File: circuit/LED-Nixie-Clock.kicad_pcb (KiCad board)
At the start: 2 copper layers, 214.6 x 43.2 mm, 197 parts, among them J1 USB Micro, J2 Debug, J3 Serial, SW1 Boot0, U1 MCP1700-3302E_SOT23, U2 STM32F103C8Tx, Y1 8MHz, Y2 32.768kHz

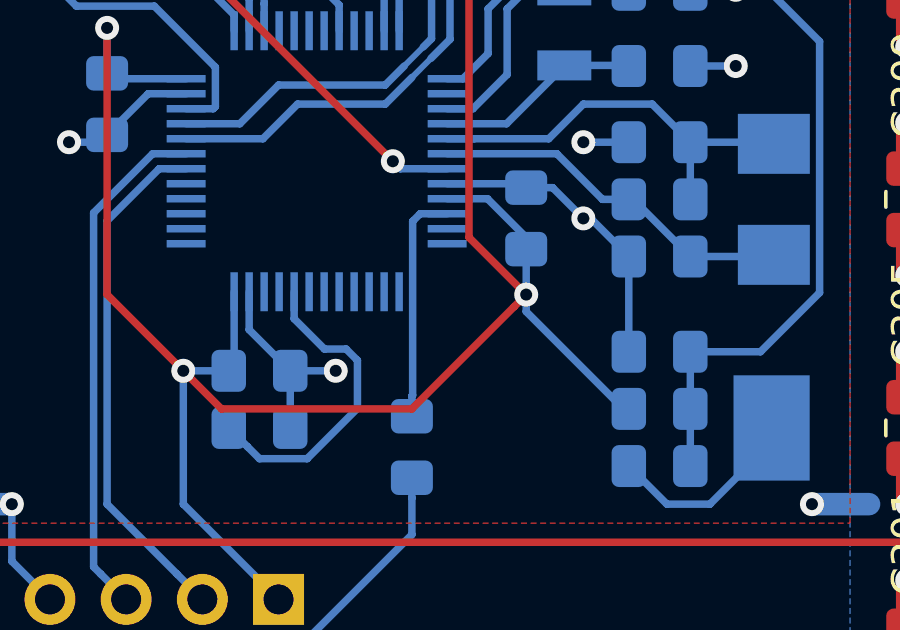
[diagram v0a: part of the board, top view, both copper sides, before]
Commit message: Move LED data bus to PA2 (which is on the same pin as USART2 Tx)
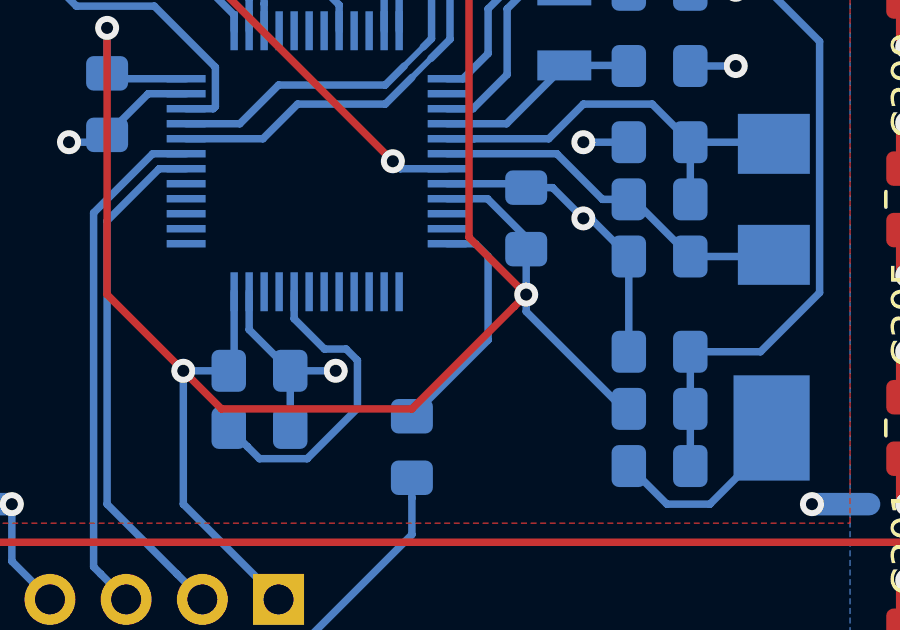
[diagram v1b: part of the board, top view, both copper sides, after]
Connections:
- U2 pad 10: Net-(R8-Pad2) -> (no net)
- U2 pad 12: (no net) -> Net-(R8-Pad2)

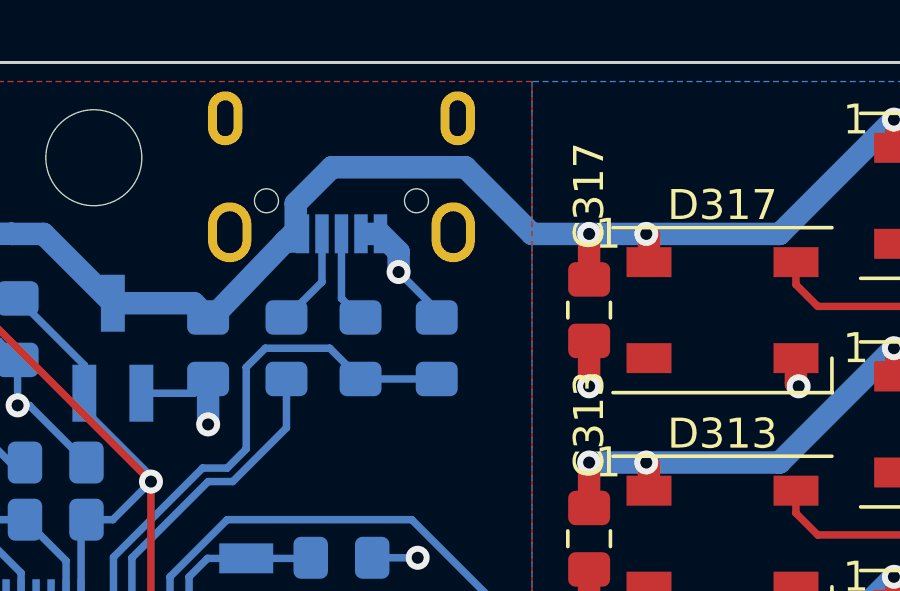
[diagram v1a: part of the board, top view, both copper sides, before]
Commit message: Fix USBDP pull up resistor
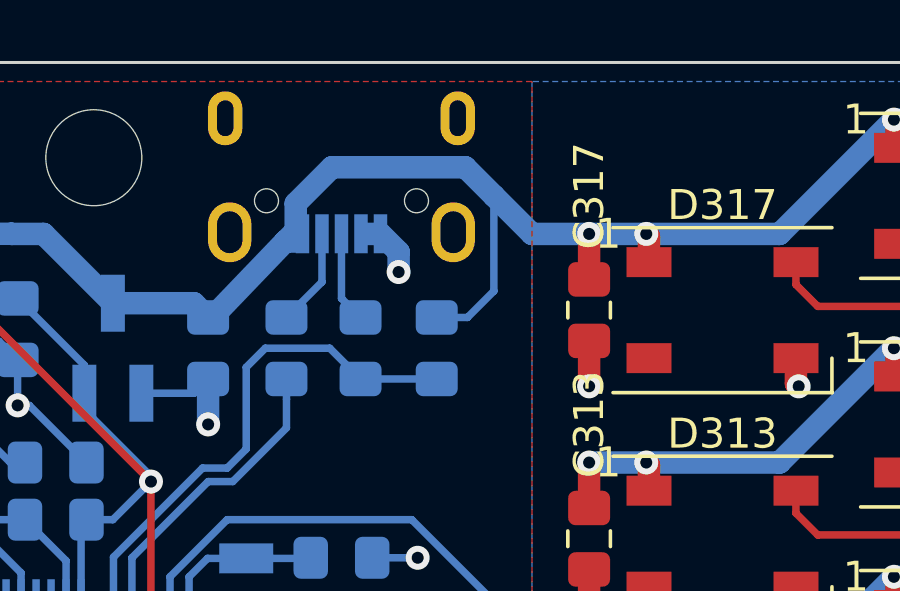
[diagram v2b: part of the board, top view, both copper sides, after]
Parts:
- turned R3 to 90 degrees
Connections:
- R3 pad 1: GND -> /USBDP
- R3 pad 2: /USBDP -> VBUS
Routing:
- net VBUS: track 1246.5 -> 1252.0 mm
- net GND: track 263.6 -> 261.5 mm
- net /USBDP: track 26.1 -> 26.7 mm
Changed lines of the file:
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@@
     (thickness 1.6)
     (drawings 262)
-    (tracks 1849)
+    (tracks 1851)
     (zones 0)
     (modules 197)
@@
   )
   (module Resistor_SMD:R_0805_2012Metric_Pad1.15x1.40mm_HandSolder (layer B.Cu)
-    (at 167.005 83.82 270)
+    (at 167.005 83.82 90)
     (descr "Resistor SMD 0805 (2012 Metric), square (rectangular) end terminal, IPC_7351 nominal with elongated pad for handsoldering. (Body size source: https://docs.google.com/spreadsheets/d/1BsfQQcO9C6DZCsRaXUlFlo91Tg2WpOkGARC1WS5S8t0/edit?usp=sharing), generated with kicad-footprint-generator")
     (tags "resistor handsolder")
     (attr smd)
-    (fp_text reference R3 (at 2.54 0 270) (layer B.SilkS)
+    (fp_text reference R3 (at 2.54 0 90) (layer B.SilkS)
       (effects (font (size 1 1) (thickness 0.15)) (justify mirror))
     )
-    (fp_text value 4.7k (at 0 -1.65 270) (layer B.Fab)
+    (fp_text value 4.7k (at 0 -1.65 90) (layer B.Fab)
       (effects (font (size 1 1) (thickness 0.15)) (justify mirror))
     )
@@
     (fp_line (start 1.85 0.95) (end 1.85 -0.95) (layer B.CrtYd) (width 0.05))
     (fp_line (start 1.85 -0.95) (end -1.85 -0.95) (layer B.CrtYd) (width 0.05))
-    (fp_text user %R (at 0 0 270) (layer B.Fab)
+    (fp_text user %R (at 0 0 90) (layer B.Fab)
       (effects (font (size 0.5 0.5) (thickness 0.08)) (justify mirror))
     )
-    (pad 1 smd roundrect (at -1.025 0 270) (size 1.15 1.4) (layers B.Cu B.Paste B.Mask) (roundrect_rratio 0.217391)
-      (net 1 GND))
-    (pad 2 smd roundrect (at 1.025 0 270) (size 1.15 1.4) (layers B.Cu B.Paste B.Mask) (roundrect_rratio 0.217391)
+    (pad 1 smd roundrect (at -1.025 0 90) (size 1.15 1.4) (layers B.Cu B.Paste B.Mask) (roundrect_rratio 0.217391)
       (net 52 /USBDP))
+    (pad 2 smd roundrect (at 1.025 0 90) (size 1.15 1.4) (layers B.Cu B.Paste B.Mask) (roundrect_rratio 0.217391)
+      (net 51 VBUS))
     (model ${KISYS3DMOD}/Resistor_SMD.3dshapes/R_0805_2012Metric.wrl
       (at (xyz 0 0 0))
@@
   (segment (start 159.385 84.845) (end 159.385 86.36) (width 0.75) (layer B.Cu) (net 1) (status 10))
   (via (at 165.735 81.28) (size 0.8) (drill 0.4) (layers F.Cu B.Cu) (net 1))
+  (segment (start 165.735 81.28) (end 165.735 80.61) (width 0.75) (layer B.Cu) (net 1))
+  (segment (start 165.735 80.61) (end 165.13 80.005) (width 0.75) (layer B.Cu) (net 1))
   (via (at 168.91 107.95) (size 0.8) (drill 0.4) (layers F.Cu B.Cu) (net 1))
   (segment (start 162.805 95.885) (end 161.29 95.885) (width 0.25) (layer B.Cu) (net 1) (status 10))
@@
   (segment (start 164.67 90.805) (end 165.345 90.805) (width 0.25) (layer B.Cu) (net 1))
   (segment (start 165.325 93.325) (end 165.345 93.345) (width 0.25) (layer B.Cu) (net 1))
-  (segment (start 165.735 80.61) (end 165.13 80.005) (width 0.75) (layer B.Cu) (net 1))
-  (segment (start 165.735 81.28) (end 165.735 80.61) (width 0.75) (layer B.Cu) (net 1))
   (segment (start 164.6555 80.01) (end 165.1 80.01) (width 0.75) (layer B.Cu) (net 1))
-  (segment (start 167.005 82.55) (end 165.735 81.28) (width 0.25) (layer B.Cu) (net 1))
-  (segment (start 167.005 82.795) (end 167.005 82.55) (width 0.25) (layer B.Cu) (net 1))
   (segment (start 158.91 85.32) (end 159.385 84.845) (width 0.25) (layer B.Cu) (net 1))
   (segment (start 157.16 85.32) (end 158.91 85.32) (width 0.25) (layer B.Cu) (net 1))
@@
   (segment (start 162.305001 78.994999) (end 162.305001 79.909399) (width 0.75) (layer B.Cu) (net 51) (status 20))
   (segment (start 163.5125 77.7875) (end 162.305001 78.994999) (width 0.75) (layer B.Cu) (net 51))
-  (segment (start 170.18 80.01) (end 167.9575 77.7875) (width 0.75) (layer B.Cu) (net 51))
   (segment (start 167.9575 77.7875) (end 163.5125 77.7875) (width 0.75) (layer B.Cu) (net 51))
   (segment (start 172.085 80.01) (end 170.18 80.01) (width 0.75) (layer B.Cu) (net 51))
@@
   (segment (start 149.438266 80.00499) (end 150.771734 80.00499) (width 0.75) (layer B.Cu) (net 51))
   (segment (start 149.433256 80.01) (end 149.438266 80.00499) (width 0.75) (layer B.Cu) (net 51))
-  (segment (start 164.465 84.845) (end 166.37 84.845) (width 0.25) (layer B.Cu) (net 52) (status 30))
+  (segment (start 168.91 78.74) (end 167.9575 77.7875) (width 0.75) (layer B.Cu) (net 51))
+  (segment (start 170.18 80.01) (end 168.91 78.74) (width 0.75) (layer B.Cu) (net 51))
+  (segment (start 168.91 81.915) (end 168.91 78.74) (width 0.25) (layer B.Cu) (net 51))
+  (segment (start 168.03 82.795) (end 168.91 81.915) (width 0.25) (layer B.Cu) (net 51))
+  (segment (start 167.005 82.795) (end 168.03 82.795) (width 0.25) (layer B.Cu) (net 51))
   (segment (start 148.05 95.27) (end 149.84 95.27) (width 0.25) (layer B.Cu) (net 52) (status 10))
   (segment (start 151.13 93.98) (end 154.686 93.98) (width 0.25) (layer B.Cu) (net 52))
@@
   (segment (start 156.23001 92.43458) (end 155.956 92.70859) (width 0.25) (layer B.Cu) (net 52))
   (segment (start 160.655 87.179989) (end 160.02 87.814989) (width 0.25) (layer B.Cu) (net 52))
+  (segment (start 164.465 84.845) (end 167.005 84.845) (width 0.25) (layer B.Cu) (net 52))
   (segment (start 163.83 82.16) (end 164.465 82.795) (width 0.25) (layer B.Cu) (net 53) (status 20))
   (segment (start 163.83 80.005) (end 163.83 82.16) (width 0.25) (layer B.Cu) (net 53) (status 10))

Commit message: Update schematic and PCB to KiCad 5.1
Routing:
- net /Digit 1/DIN: track 115.4 -> 116.1 mm
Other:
- net class Power: trace_width 0.75 -> 0.5

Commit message: Adjust credits text on PCB
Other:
- board text added: "LED Nixie Clock"
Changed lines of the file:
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@@
   (general
     (thickness 1.6)
-    (drawings 262)
+    (drawings 263)
     (tracks 1849)
     (zones 0)
@@
     )
   )
+  (gr_text "LED Nixie Clock" (at 140.462 114.046) (layer B.SilkS)
+    (effects (font (size 1 0.5) (thickness 0.1)) (justify left mirror))
+  )
   (gr_line (start 89.75 81.15) (end 89.75 83.95) (layer Dwgs.User) (width 0.2))
   (gr_line (start 49.95 81.15) (end 89.75 81.15) (layer Dwgs.User) (width 0.2))
@@
   (gr_line (start 145.415 79.8195) (end 145.415 90.3605) (layer Dwgs.User) (width 0.1))
   (gr_line (start 143.8275 85.09) (end 146.8755 85.09) (layer Dwgs.User) (width 0.1))
-  (gr_text github.com/zargony/led-nixie-clock (at 133.35 115.57) (layer B.SilkS)
-    (effects (font (size 1 0.5) (thickness 0.1)) (justify mirror))
+  (gr_text github.com/zargony/led-nixie-clock (at 140.462 115.57) (layer B.SilkS)
+    (effects (font (size 1 0.5) (thickness 0.1)) (justify left mirror))
   )
   (gr_line (start 220.98 74.295) (end 220.98 117.475) (layer F.CrtYd) (width 0.1))

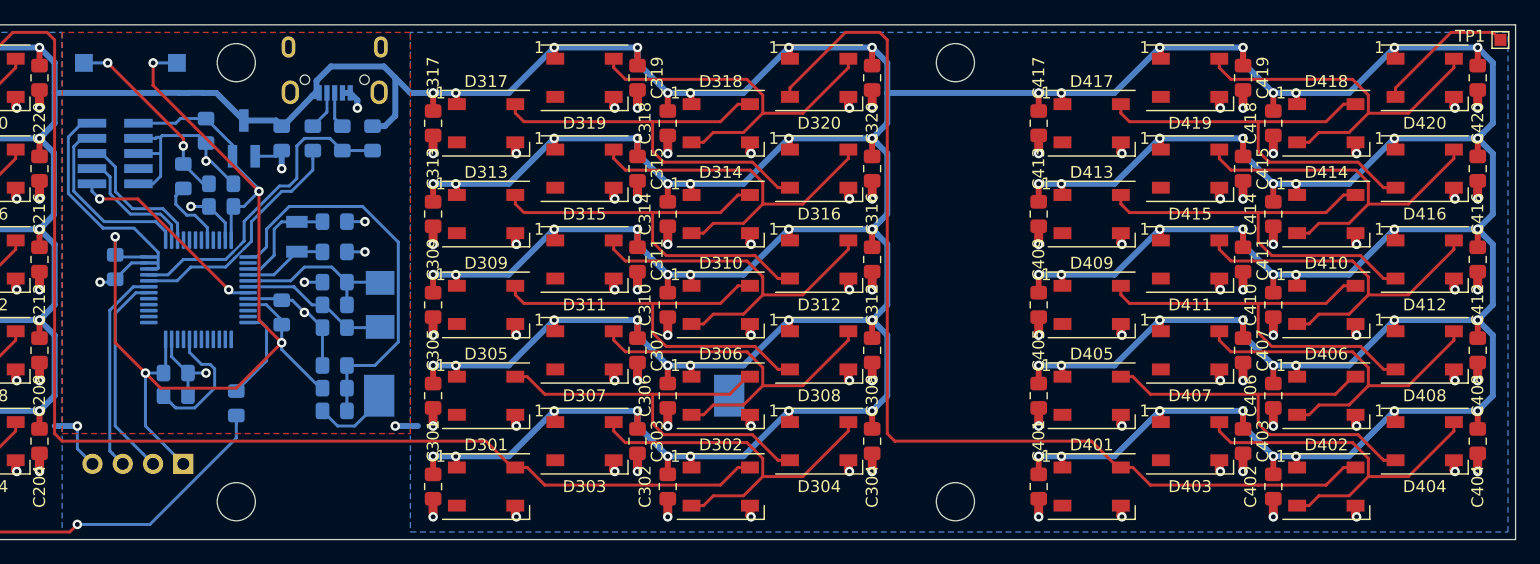
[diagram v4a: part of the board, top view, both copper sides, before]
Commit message: Add test points for DIN and DOUT, improve front side routing
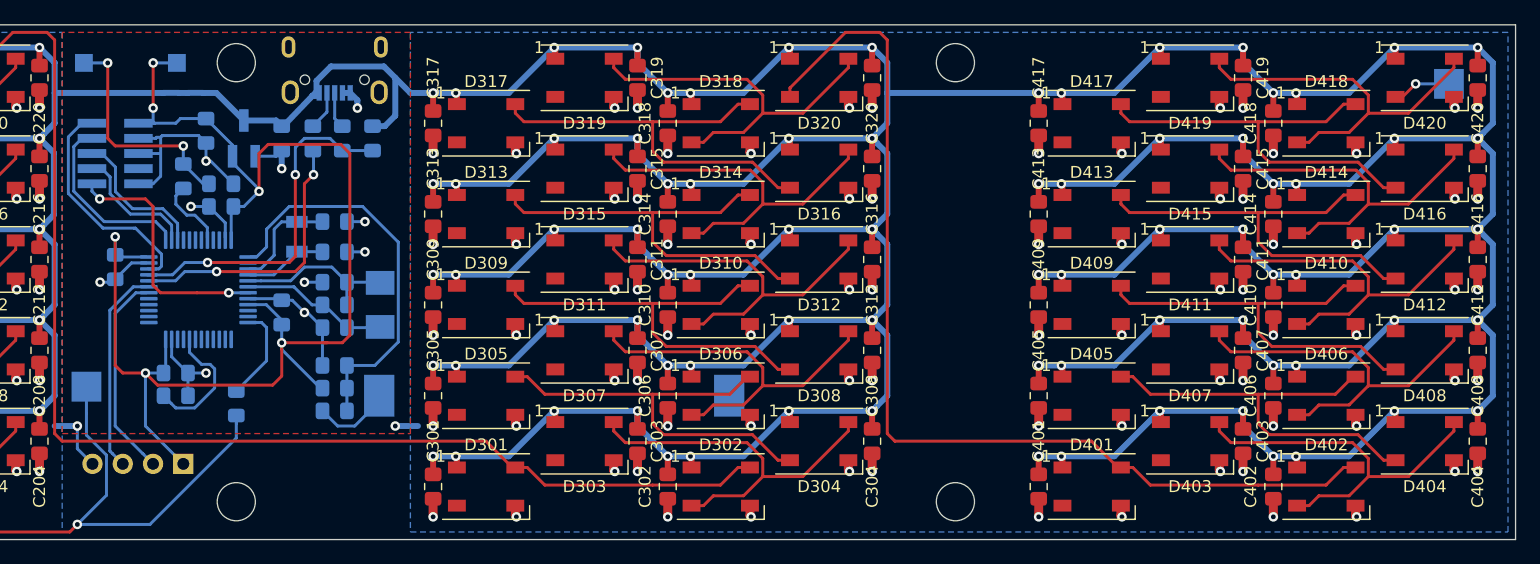
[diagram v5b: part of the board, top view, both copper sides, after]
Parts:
- removed TP1: DOUT, TestPoint:TestPoint_Pad_1.0x1.0mm
- added DIN: DIN, TestPoint:TestPoint_Pad_2.5x2.5mm, B.Cu at (143.0, 104.6)
- added DOUT: DOUT, TestPoint:TestPoint_Pad_2.5x2.5mm, B.Cu at (257.3, 79.2)
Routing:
- net /Digit 1/DIN: track 116.1 -> 129.4 mm
- net VDD: track 102.9 -> 115.5 mm, vias 5 -> 6
- net /Digit 4/DOUT: track 11.7 -> 4.93 mm, vias 0 -> 1
- net /RESET: track 17.4 -> 21.3 mm
- net Net-(R5-Pad2): track 15.9 -> 19.3 mm
- net /USBDM: track 20.4 -> 23.6 mm, vias 0 -> 2
- net /USBDP: track 26.7 -> 29.5 mm, vias 0 -> 2

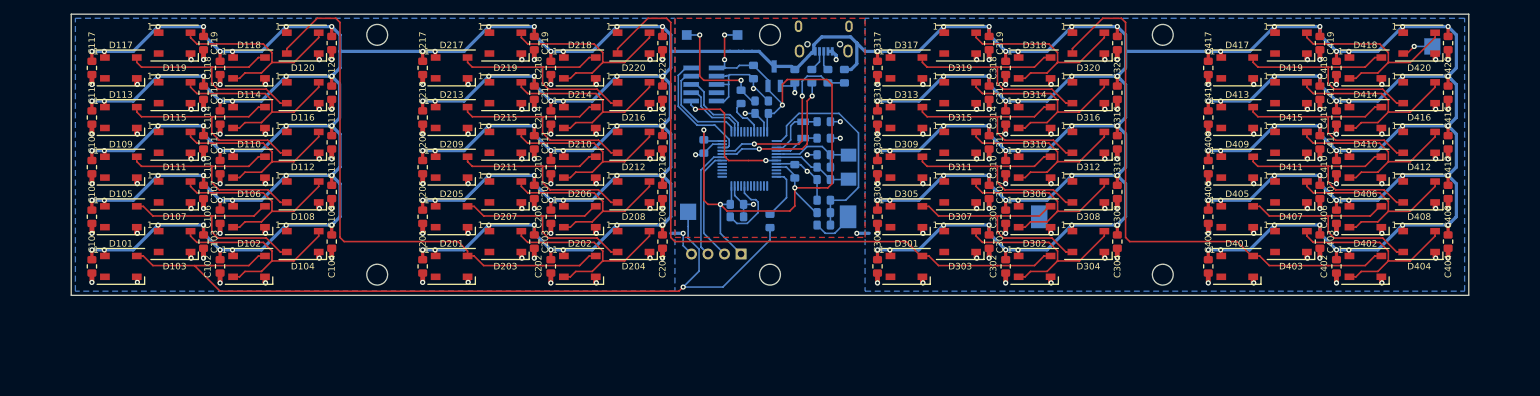
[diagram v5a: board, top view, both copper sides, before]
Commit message: Add input buttons
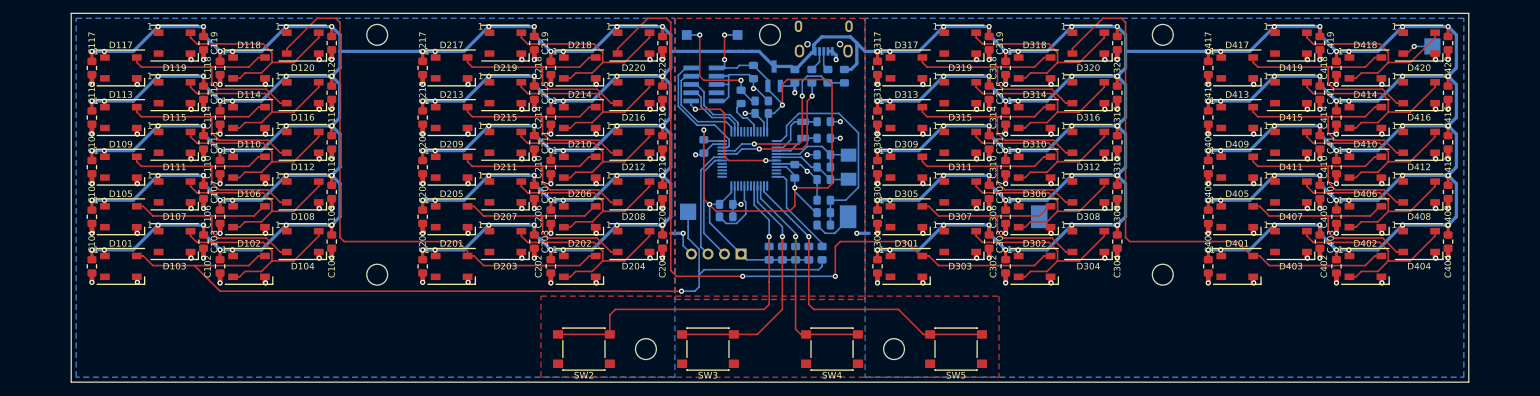
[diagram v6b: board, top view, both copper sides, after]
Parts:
- removed DIN: DIN, TestPoint:TestPoint_Pad_2.5x2.5mm
- added H7: MountingHole, MountingHole:MountingHole_3.2mm_M3_ISO7380, F.Cu at (174.6, 125.7)
- added R10: 100k, Resistor_SMD:R_0805_2012Metric_Pad1.15x1.40mm_HandSolder, B.Cu at (157.5, 111.0)
- added R11: 100k, Resistor_SMD:R_0805_2012Metric_Pad1.15x1.40mm_HandSolder, B.Cu at (159.5, 111.0)
- added R12: 100k, Resistor_SMD:R_0805_2012Metric_Pad1.15x1.40mm_HandSolder, B.Cu at (161.5, 111.0)
- added R9: 100k, Resistor_SMD:R_0805_2012Metric_Pad1.15x1.40mm_HandSolder, B.Cu at (155.4, 111.0)
- added SW2: Button "Back", Button_Switch_SMD:SW_Push_1P1T_NO_6x6mm_H9.5mm, F.Cu at (127.0, 125.7)
- added SW3: Button "-", Button_Switch_SMD:SW_Push_1P1T_NO_6x6mm_H9.5mm, F.Cu at (146.1, 125.7)
- added SW4: Button "+", Button_Switch_SMD:SW_Push_1P1T_NO_6x6mm_H9.5mm, F.Cu at (165.1, 125.7)
- added SW5: Button "Ok", Button_Switch_SMD:SW_Push_1P1T_NO_6x6mm_H9.5mm, F.Cu at (184.2, 125.7)
- added TP1: DIN, TestPoint:TestPoint_Pad_2.5x2.5mm, B.Cu at (143.0, 104.6)
- moved H6 80.2 mm to (136.5, 125.7)
- moved H2 70.7 mm to (155.6, 77.5)
- moved H3 60.3 mm to (215.9, 77.5)
- moved H4 60.3 mm to (95.2, 114.3)
- moved H5 36.8 mm to (215.9, 114.3)
- moved R8 9.41 mm to (163.6, 111.0)
- moved C7 1.65 mm to (148.8, 103.5)
- moved R7 1.65 mm to (148.8, 105.4)
- renumbered DOUT to TP2
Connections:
- U2 pad 14: (no net) -> /BTN3
- U2 pad 15: (no net) -> /BTN2
- U2 pad 16: (no net) -> /BTN1
- U2 pad 17: (no net) -> /BTN0
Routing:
- net /BTN0: track 0.00 -> 56.7 mm, vias 0 -> 1
- net /BTN3: track 0.00 -> 51.0 mm, vias 0 -> 1
- net /BTN1: track 0.00 -> 39.1 mm, vias 0 -> 1
- net /BTN2: track 0.00 -> 35.6 mm, vias 0 -> 1
- net VDD: track 115.5 -> 127.7 mm
- net /Digit 3/DIN: track 104.9 -> 114.9 mm, vias 0 -> 2
- net Net-(R8-Pad2): track 7.92 -> 14.3 mm
- net /Digit 1/DIN: track 129.4 -> 132.9 mm
- net /BOOT1: track 10.6 -> 9.46 mm
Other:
- board size 214.6 x 43.2 mm -> 214.6 x 56.6 mm

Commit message: Enlarge PCB and add more mounting holes
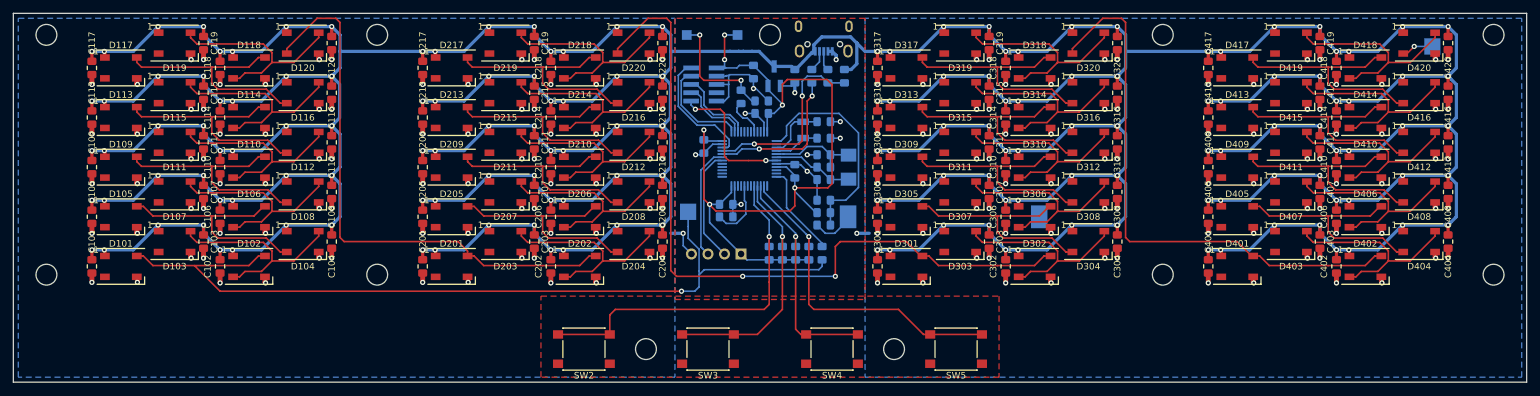
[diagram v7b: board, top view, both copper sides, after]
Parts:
- added H1: MountingHole, MountingHole:MountingHole_3.2mm_M3_ISO7380, F.Cu at (44.5, 77.5)
- added H5: MountingHole, MountingHole:MountingHole_3.2mm_M3_ISO7380, F.Cu at (266.7, 77.5)
- added H6: MountingHole, MountingHole:MountingHole_3.2mm_M3_ISO7380, F.Cu at (44.5, 114.3)
- added H9: MountingHole, MountingHole:MountingHole_3.2mm_M3_ISO7380, F.Cu at (266.7, 114.3)
- renumbered H6 to H10, H7 to H11, H1 to H2, H2 to H3, H3 to H4, H4 to H7, H5 to H8
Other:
- board size 214.6 x 56.6 mm -> 232.4 x 56.6 mm
